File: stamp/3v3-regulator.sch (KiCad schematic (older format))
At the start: 3 parts

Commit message: Pre-review
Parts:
- C3, C4: renamed from C?; footprint Capacitor_SMD:C_0402_1005Metric -> Capacitor_SMD:C_0603_1608Metric
- gave numbers to parts that had none: 1
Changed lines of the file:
@@
 AR Path="/5FC8F2FB" Ref="U?"  Part="1"
 AR Path="/5FA2108C/5FC8F2FB" Ref="U?"  Part="1"
-F 0 "U?" H 5300 3292 50  0000 C CNN
+AR Path="/5FC8E9A5/5FC8F2FB" Ref="U1"  Part="1"
+F 0 "U1" H 5300 3292 50  0000 C CNN
 F 1 "AP2112K-3.3" H 5300 3201 50  0000 C CNN
 F 2 "Package_TO_SOT_SMD:SOT-23-5" H 5300 3275 50  0001 C CNN
@@
 $EndComp
 $Comp
-L power:GND #PWR?
+L power:GND #PWR0107
 U 1 1 5FC8F301
 P 5300 3250
-F 0 "#PWR?" H 5300 3000 50  0001 C CNN
+F 0 "#PWR0107" H 5300 3000 50  0001 C CNN
 F 1 "GND" H 5305 3077 50  0000 C CNN
 F 2 "" H 5300 3250 50  0001 C CNN
@@
 	1    0    0    -1
 $EndComp
-Text Label 3250 3000 2    50   ~ 0
+Text Label 3250 2850 2    50   ~ 0
 VMAX
-Text Label 3250 3500 2    50   ~ 0
+Text Label 3250 2950 2    50   ~ 0
 3v3_EN
 Text Label 6150 2850 0    50   ~ 0
@@
 +3v3 Regulator
 $Comp
-L Device:C C?
+L Device:C C3
 U 1 1 5FC8F30B
 P 4950 3650
-F 0 "C?" H 5065 3696 50  0000 L CNN
+F 0 "C3" H 5065 3696 50  0000 L CNN
 F 1 "1uF" H 5065 3605 50  0000 L CNN
-F 2 "Capacitor_SMD:C_0402_1005Metric" H 4988 3500 50  0001 C CNN
+F 2 "Capacitor_SMD:C_0603_1608Metric" H 4988 3500 50  0001 C CNN
 F 3 "~" H 4950 3650 50  0001 C CNN
 	1    4950 3650
@@
 $EndComp
 $Comp
-L Device:C C?
+L Device:C C4
 U 1 1 5FC8F311
 P 5700 3650
-F 0 "C?" H 5815 3696 50  0000 L CNN
+F 0 "C4" H 5815 3696 50  0000 L CNN
 F 1 "1uF" H 5815 3605 50  0000 L CNN
-F 2 "Capacitor_SMD:C_0402_1005Metric" H 5738 3500 50  0001 C CNN
+F 2 "Capacitor_SMD:C_0603_1608Metric" H 5738 3500 50  0001 C CNN
 F 3 "~" H 5700 3650 50  0001 C CNN
 	1    5700 3650
@@
 $EndComp
 $Comp
-L power:GND #PWR?
+L power:GND #PWR0108
 U 1 1 5FC8F317
 P 5350 3800
-F 0 "#PWR?" H 5350 3550 50  0001 C CNN
+F 0 "#PWR0108" H 5350 3550 50  0001 C CNN
 F 1 "GND" H 5355 3627 50  0000 C CNN
 F 2 "" H 5350 3800 50  0001 C CNN
@@
 Connection ~ 5700 2850
 Wire Wire Line
-	3800 2850 3800 3000
-Wire Wire Line
-	4150 3500 4150 2950
-Wire Wire Line
-	3800 2850 4950 2850
-Wire Wire Line
 	5700 2850 6150 2850
 Wire Wire Line
 	4950 2850 4950 3500
-Wire Wire Line
-	4150 2950 5000 2950
-Wire Wire Line
-	3250 3000 3800 3000
-Wire Wire Line
-	3250 3500 4150 3500
 Text HLabel 950  700  0    50   Input ~ 0
 VMAX
@@
 +3v3
 $Comp
-L power:GND #PWR?
+L power:GND #PWR0109
 U 1 1 5FC90131
 P 1250 1000
-F 0 "#PWR?" H 1250 750 50  0001 C CNN
+F 0 "#PWR0109" H 1250 750 50  0001 C CNN
 F 1 "GND" H 1255 827 50  0000 C CNN
 F 2 "" H 1250 1000 50  0001 C CNN
@@
 Wire Wire Line
 	950  1000 1250 1000
+Wire Wire Line
+	3250 2850 4950 2850
+Wire Wire Line
+	3250 2950 5000 2950
 $EndSCHEMATC

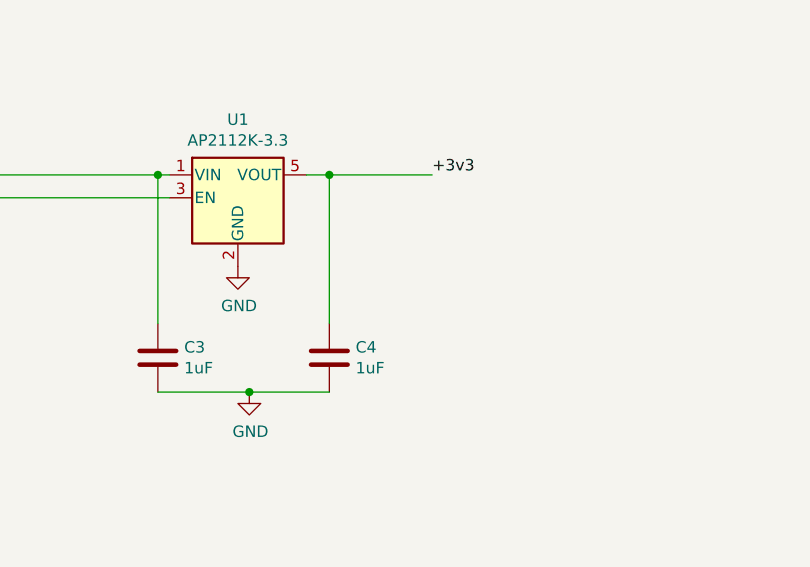
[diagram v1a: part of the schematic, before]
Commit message: Add more filter caps
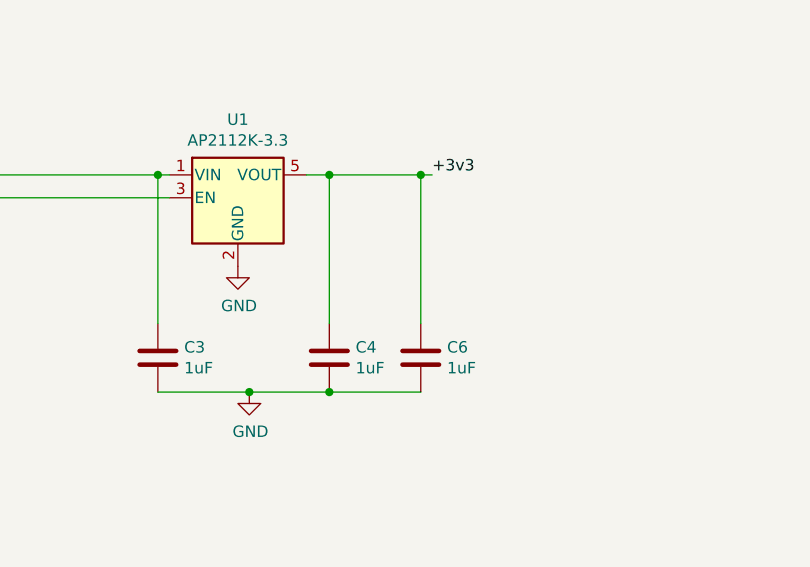
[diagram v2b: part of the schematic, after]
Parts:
- added C6: 1uF, Capacitor_SMD:C_0603_1608Metric, symbol Device:C
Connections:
- net +3v3: now also C6.1
- net GND: now also C6.2
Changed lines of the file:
@@
 Connection ~ 5700 2850
 Wire Wire Line
-	5700 2850 6150 2850
+	5700 2850 6100 2850
 Wire Wire Line
 	4950 2850 4950 3500
@@
 Wire Wire Line
 	3250 2950 5000 2950
+$Comp
+L Device:C C6
+U 1 1 5FC4F6F8
+P 6100 3650
+F 0 "C6" H 6215 3696 50  0000 L CNN
+F 1 "1uF" H 6215 3605 50  0000 L CNN
+F 2 "Capacitor_SMD:C_0603_1608Metric" H 6138 3500 50  0001 C CNN
+F 3 "~" H 6100 3650 50  0001 C CNN
+	1    6100 3650
+	1    0    0    -1
+$EndComp
+Wire Wire Line
+	5700 3800 6100 3800
+Connection ~ 5700 3800
+Wire Wire Line
+	6100 3500 6100 2850
+Connection ~ 6100 2850
+Wire Wire Line
+	6100 2850 6150 2850
 $EndSCHEMATC
